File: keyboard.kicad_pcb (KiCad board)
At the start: 2 copper layers, 359.9 x 94.6 mm, 210 parts, among them IC1 ATMEGA32U4, J1 USB C, X1 ASX3F

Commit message: Add an additional led to PCB
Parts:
- added D102: WS2812B, LED_SMD:LED_WS2812B_PLCC4_5.0x5.0mm_P3.2mm, B.Cu at (408.9, 121.2)
- moved D91 18.2 mm to (81.3, 119.4)
- moved D8 11.5 mm to (102.0, 105.2)
- moved D89 10.3 mm to (352.1, 154.2)
- moved D90 9.73 mm to (119.1, 140.5)
- moved D34 6.42 mm to (191.6, 135.6)
- moved D100 5.68 mm to (233.9, 140.5)
- moved D99 4.72 mm to (290.8, 140.3)
- moved D98 3.63 mm to (349.2, 140.3)
- moved C6 1.35 mm to (169.7, 155.3)
- moved D101 0.54 mm to (178.8, 140.5)
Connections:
- D97 pad 2: Net-(D97-Pad2) -> Net-(D102-Pad4)
- D98 pad 4: Net-(D97-Pad2) -> Net-(D102-Pad2)
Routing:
- net VCC: track 568.0 -> 912.6 mm, vias 8 -> 18
- net Net-(D102-Pad2): track 0.00 -> 70.3 mm, vias 0 -> 2
- net Net-(D100-Pad4): track 0.00 -> 57.9 mm, vias 0 -> 2
- net Net-(D98-Pad2): track 0.00 -> 54.8 mm, vias 0 -> 2
- net Net-(D102-Pad4): track 0.00 -> 49.1 mm
- net Net-(D100-Pad2): track 0.00 -> 47.8 mm, vias 0 -> 1
- net /col16: track 348.1 -> 333.7 mm, vias 4 -> 3
- net Net-(D8-Pad2): track 16.2 -> 5.02 mm
- net Net-(D89-Pad2): track 4.11 -> 14.8 mm
- net /col15: track 306.8 -> 297.4 mm, vias 4 -> 3
- net /row4: track 418.3 -> 410.0 mm
- net Net-(D34-Pad2): track 15.8 -> 10.5 mm
- net /col14: track 308.1 -> 303.5 mm
- net /col4: track 100.1 -> 102.4 mm
- net /col2: track 160.3 -> 162.4 mm
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
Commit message: Finish connecting all leds
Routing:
- net Net-(D91-Pad2): track 0.00 -> 65.2 mm, vias 0 -> 2
- net Net-(D90-Pad2): track 0.00 -> 40.4 mm, vias 0 -> 2
- net /leds: track 0.00 -> 36.2 mm, vias 0 -> 2
- net /col16: track 333.7 -> 343.1 mm, vias 3 -> 4
- net /col15: track 297.4 -> 306.0 mm, vias 3 -> 4
- net Net-(D100-Pad2): track 47.8 -> 52.3 mm, vias 1 -> 2
- net /col4: track 102.4 -> 104.8 mm

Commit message: Make first row linear
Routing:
- net /row1: track 459.8 -> 406.4 mm

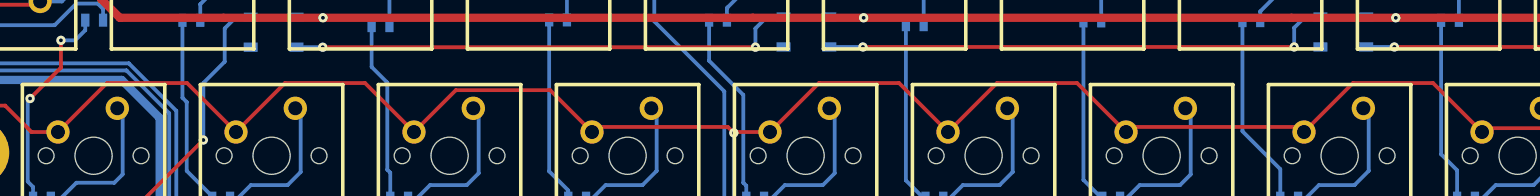
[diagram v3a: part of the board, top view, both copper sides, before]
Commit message: Make second row linear
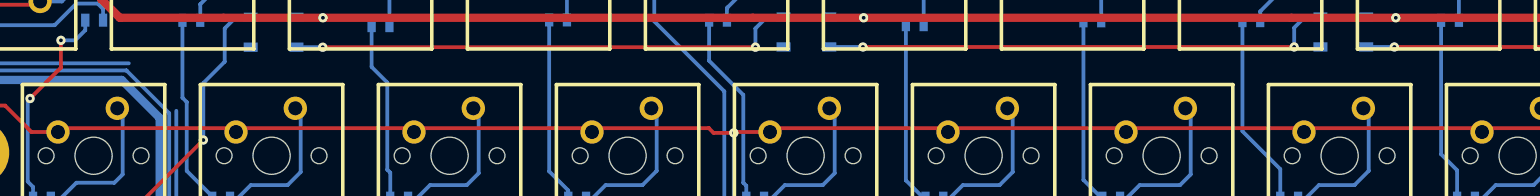
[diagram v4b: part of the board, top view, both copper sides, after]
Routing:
- net /row2: track 409.4 -> 386.6 mm
- net Net-(IC1-Pad4): track 123.8 -> 116.6 mm
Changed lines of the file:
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@@
     (thickness 1.6002)
     (drawings 87)
-    (tracks 1705)
+    (tracks 1713)
     (zones 0)
     (modules 211)
@@
   (segment (start 324.38848 70.866) (end 324.8025 71.28002) (width 0.4064) (layer F.Cu) (net 71))
   (segment (start 296.926 70.866) (end 324.38848 70.866) (width 0.4064) (layer F.Cu) (net 71))
-  (segment (start 96.2025 90.33002) (end 101.44252 85.09) (width 0.4064) (layer F.Cu) (net 72))
-  (segment (start 110.01248 85.09) (end 115.2525 90.33002) (width 0.4064) (layer F.Cu) (net 72))
-  (segment (start 205.26248 85.09) (end 210.5025 90.33002) (width 0.4064) (layer F.Cu) (net 72))
-  (segment (start 120.49252 85.09) (end 129.06248 85.09) (width 0.4064) (layer F.Cu) (net 72))
-  (segment (start 129.06248 85.09) (end 134.3025 90.33002) (width 0.4064) (layer F.Cu) (net 72))
-  (segment (start 138.78052 85.852) (end 148.87448 85.852) (width 0.4064) (layer F.Cu) (net 72))
-  (segment (start 148.87448 85.852) (end 153.3525 90.33002) (width 0.4064) (layer F.Cu) (net 72))
-  (segment (start 191.4525 90.33002) (end 196.69252 85.09) (width 0.4064) (layer F.Cu) (net 72))
-  (segment (start 101.44252 85.09) (end 110.01248 85.09) (width 0.4064) (layer F.Cu) (net 72))
-  (segment (start 134.3025 90.33002) (end 138.78052 85.852) (width 0.4064) (layer F.Cu) (net 72))
-  (segment (start 196.69252 85.09) (end 205.26248 85.09) (width 0.4064) (layer F.Cu) (net 72))
-  (segment (start 172.4025 90.33002) (end 177.64252 85.09) (width 0.4064) (layer F.Cu) (net 72))
-  (segment (start 186.21248 85.09) (end 191.4525 90.33002) (width 0.4064) (layer F.Cu) (net 72))
-  (segment (start 177.64252 85.09) (end 186.21248 85.09) (width 0.4064) (layer F.Cu) (net 72))
-  (segment (start 115.2525 90.33002) (end 120.49252 85.09) (width 0.4064) (layer F.Cu) (net 72))
-  (segment (start 234.79252 85.09) (end 243.36248 85.09) (width 0.4064) (layer F.Cu) (net 72))
-  (segment (start 229.5525 90.33002) (end 234.79252 85.09) (width 0.4064) (layer F.Cu) (net 72))
-  (segment (start 243.36248 85.09) (end 248.6025 90.33002) (width 0.4064) (layer F.Cu) (net 72))
   (segment (start 93.37802 90.33002) (end 96.2025 90.33002) (width 0.4064) (layer F.Cu) (net 72))
   (segment (start 72.39 90.33002) (end 72.93102 89.789) (width 0.4064) (layer F.Cu) (net 72))
@@
   (segment (start 172.4025 90.33002) (end 168.62298 90.33002) (width 0.4064) (layer F.Cu) (net 72))
   (segment (start 168.529 90.424) (end 168.62298 90.33002) (width 0.4064) (layer F.Cu) (net 72))
-  (segment (start 153.89352 89.789) (end 167.894 89.789) (width 0.4064) (layer F.Cu) (net 72))
-  (segment (start 167.894 89.789) (end 168.529 90.424) (width 0.4064) (layer F.Cu) (net 72))
-  (segment (start 153.3525 90.33002) (end 153.89352 89.789) (width 0.4064) (layer F.Cu) (net 72))
-  (segment (start 211.04352 89.789) (end 229.01148 89.789) (width 0.4064) (layer F.Cu) (net 72))
-  (segment (start 229.01148 89.789) (end 229.5525 90.33002) (width 0.4064) (layer F.Cu) (net 72))
   (segment (start 210.5025 90.33002) (end 211.04352 89.789) (width 0.4064) (layer F.Cu) (net 72))
   (segment (start 249.01652 89.916) (end 267.23848 89.916) (width 0.4064) (layer F.Cu) (net 72))
@@
   (segment (start 390.0805 89.9795) (end 390.525 90.424) (width 0.4064) (layer F.Cu) (net 72))
   (segment (start 372.0465 89.9795) (end 390.0805 89.9795) (width 0.4064) (layer F.Cu) (net 72))
+  (segment (start 96.2025 90.33002) (end 96.2025 90.2335) (width 0.4064) (layer F.Cu) (net 72))
+  (segment (start 96.2025 90.2335) (end 96.52 89.916) (width 0.4064) (layer F.Cu) (net 72))
+  (segment (start 114.83848 89.916) (end 115.2525 90.33002) (width 0.4064) (layer F.Cu) (net 72))
+  (segment (start 96.52 89.916) (end 114.83848 89.916) (width 0.4064) (layer F.Cu) (net 72))
+  (segment (start 248.6025 90.33002) (end 248.06402 90.33002) (width 0.4064) (layer F.Cu) (net 72))
+  (segment (start 248.06402 90.33002) (end 247.65 89.916) (width 0.4064) (layer F.Cu) (net 72))
+  (segment (start 247.65 89.916) (end 229.96652 89.916) (width 0.4064) (layer F.Cu) (net 72))
+  (segment (start 229.96652 89.916) (end 229.5525 90.33002) (width 0.4064) (layer F.Cu) (net 72))
+  (segment (start 229.5525 90.33002) (end 229.52202 90.33002) (width 0.4064) (layer F.Cu) (net 72))
+  (segment (start 229.52202 90.33002) (end 229.108 89.916) (width 0.4064) (layer F.Cu) (net 72))
+  (segment (start 210.91652 89.916) (end 210.5025 90.33002) (width 0.4064) (layer F.Cu) (net 72))
+  (segment (start 229.108 89.916) (end 210.91652 89.916) (width 0.4064) (layer F.Cu) (net 72))
+  (segment (start 210.5025 90.33002) (end 209.96402 90.33002) (width 0.4064) (layer F.Cu) (net 72))
+  (segment (start 209.96402 90.33002) (end 209.55 89.916) (width 0.4064) (layer F.Cu) (net 72))
+  (segment (start 191.86652 89.916) (end 191.4525 90.33002) (width 0.4064) (layer F.Cu) (net 72))
+  (segment (start 209.55 89.916) (end 191.86652 89.916) (width 0.4064) (layer F.Cu) (net 72))
+  (segment (start 172.81652 89.916) (end 172.4025 90.33002) (width 0.4064) (layer F.Cu) (net 72))
+  (segment (start 190.754 89.916) (end 172.81652 89.916) (width 0.4064) (layer F.Cu) (net 72))
+  (segment (start 191.16802 90.33002) (end 190.754 89.916) (width 0.4064) (layer F.Cu) (net 72))
+  (segment (start 191.4525 90.33002) (end 191.16802 90.33002) (width 0.4064) (layer F.Cu) (net 72))
+  (segment (start 153.76652 89.916) (end 153.3525 90.33002) (width 0.4064) (layer F.Cu) (net 72))
+  (segment (start 165.862 89.916) (end 153.76652 89.916) (width 0.4064) (layer F.Cu) (net 72))
+  (segment (start 166.37 90.424) (end 165.862 89.916) (width 0.4064) (layer F.Cu) (net 72))
+  (segment (start 168.529 90.424) (end 166.37 90.424) (width 0.4064) (layer F.Cu) (net 72))
+  (segment (start 134.71652 89.916) (end 134.3025 90.33002) (width 0.4064) (layer F.Cu) (net 72))
+  (segment (start 152.908 89.916) (end 134.71652 89.916) (width 0.4064) (layer F.Cu) (net 72))
+  (segment (start 153.32202 90.33002) (end 152.908 89.916) (width 0.4064) (layer F.Cu) (net 72))
+  (segment (start 153.3525 90.33002) (end 153.32202 90.33002) (width 0.4064) (layer F.Cu) (net 72))
+  (segment (start 134.3025 90.33002) (end 134.01802 90.33002) (width 0.4064) (layer F.Cu) (net 72))
+  (segment (start 134.01802 90.33002) (end 133.604 89.916) (width 0.4064) (layer F.Cu) (net 72))
+  (segment (start 115.66652 89.916) (end 115.2525 90.33002) (width 0.4064) (layer F.Cu) (net 72))
+  (segment (start 133.604 89.916) (end 115.66652 89.916) (width 0.4064) (layer F.Cu) (net 72))
   (segment (start 100.69068 108.95584) (end 100.965 109.38002) (width 0.4064) (layer F.Cu) (net 73))
   (segment (start 106.20502 104.14) (end 114.77498 104.14) (width 0.4064) (layer F.Cu) (net 73))
@@
   (segment (start 159.68472 139.99972) (end 157.90926 138.22426) (width 0.4064) (layer B.Cu) (net 76))
   (segment (start 159.68472 139.99972) (end 159.68472 143.19504) (width 0.4064) (layer B.Cu) (net 76))
-  (segment (start 108.86694 88.05926) (end 103.78694 82.97926) (width 0.4064) (layer B.Cu) (net 76))
   (segment (start 114.45494 106.09326) (end 114.45494 116.76126) (width 0.4064) (layer B.Cu) (net 76))
   (segment (start 114.45494 116.76126) (end 124.10694 126.41326) (width 0.4064) (layer B.Cu) (net 76))

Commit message: Make third row linear
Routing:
- net /row3: track 438.0 -> 415.5 mm
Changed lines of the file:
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@@
   (layers
     (0 F.Cu signal)
-    (31 B.Cu signal)
+    (31 B.Cu signal hide)
     (32 B.Adhes user hide)
     (33 F.Adhes user hide)
@@
   (segment (start 133.604 89.916) (end 115.66652 89.916) (width 0.4064) (layer F.Cu) (net 72))
   (segment (start 100.69068 108.95584) (end 100.965 109.38002) (width 0.4064) (layer F.Cu) (net 73))
-  (segment (start 106.20502 104.14) (end 114.77498 104.14) (width 0.4064) (layer F.Cu) (net 73))
-  (segment (start 100.965 109.38002) (end 106.20502 104.14) (width 0.4064) (layer F.Cu) (net 73))
-  (segment (start 133.82498 104.14) (end 139.065 109.38002) (width 0.4064) (layer F.Cu) (net 73))
-  (segment (start 286.22498 104.14) (end 291.465 109.38002) (width 0.4064) (layer F.Cu) (net 73))
-  (segment (start 258.60502 104.14) (end 267.17498 104.14) (width 0.4064) (layer F.Cu) (net 73))
-  (segment (start 277.65502 104.14) (end 286.22498 104.14) (width 0.4064) (layer F.Cu) (net 73))
-  (segment (start 253.365 109.38002) (end 258.60502 104.14) (width 0.4064) (layer F.Cu) (net 73))
   (segment (start 101.522711 109.601) (end 100.965 109.38002) (width 0.4064) (layer F.Cu) (net 73))
   (segment (start 100.965 109.38002) (end 100.69068 108.93552) (width 0.4064) (layer F.Cu) (net 73))
-  (segment (start 125.25502 104.14) (end 133.82498 104.14) (width 0.4064) (layer F.Cu) (net 73))
-  (segment (start 114.77498 104.14) (end 120.015 109.38002) (width 0.4064) (layer F.Cu) (net 73))
-  (segment (start 267.17498 104.14) (end 272.415 109.38002) (width 0.4064) (layer F.Cu) (net 73))
-  (segment (start 120.015 109.38002) (end 125.25502 104.14) (width 0.4064) (layer F.Cu) (net 73))
-  (segment (start 272.415 109.38002) (end 277.65502 104.14) (width 0.4064) (layer F.Cu) (net 73))
   (segment (start 74.77252 109.38002) (end 74.77252 108.42752) (width 0.4064) (layer F.Cu) (net 73) (status 30))
   (segment (start 322.42125 109.37875) (end 322.707 109.6645) (width 0.4064) (layer F.Cu) (net 73))
-  (segment (start 171.56176 116.06276) (end 171.577 116.04752) (width 0.4064) (layer B.Cu) (net 73))
   (segment (start 167.05326 120.57126) (end 171.56176 116.06276) (width 0.4064) (layer B.Cu) (net 73))
   (segment (start 171.577 108.966) (end 176.75098 108.966) (width 0.4064) (layer F.Cu) (net 73))
   (segment (start 176.75098 108.966) (end 177.165 109.38002) (width 0.4064) (layer F.Cu) (net 73))
-  (segment (start 158.52902 108.966) (end 171.577 108.966) (width 0.4064) (layer F.Cu) (net 73))
+  (segment (start 158.52902 108.966) (end 171.45 108.966) (width 0.4064) (layer F.Cu) (net 73))
   (segment (start 158.115 109.38002) (end 158.52902 108.966) (width 0.4064) (layer F.Cu) (net 73))
-  (segment (start 171.56176 108.56976) (end 171.45 108.458) (width 0.4064) (layer B.Cu) (net 73))
-  (via (at 171.45 108.458) (size 1) (layers F.Cu B.Cu) (net 73))
-  (segment (start 171.45 108.458) (end 171.577 108.585) (width 0.4064) (layer F.Cu) (net 73))
-  (segment (start 171.577 108.585) (end 171.577 108.966) (width 0.4064) (layer F.Cu) (net 73))
-  (segment (start 171.56176 116.06276) (end 171.56176 108.56976) (width 0.4064) (layer B.Cu) (net 73))
   (segment (start 234.72902 108.966) (end 252.95098 108.966) (width 0.4064) (layer F.Cu) (net 73))
   (segment (start 252.95098 108.966) (end 253.365 109.38002) (width 0.4064) (layer F.Cu) (net 73))
@@
   (segment (start 157.70098 108.966) (end 158.115 109.38002) (width 0.4064) (layer F.Cu) (net 73))
   (segment (start 139.065 109.38002) (end 139.47902 108.966) (width 0.4064) (layer F.Cu) (net 73))
-  (segment (start 74.77252 109.38002) (end 76.2 107.95254) (width 0.4064) (layer F.Cu) (net 73))
-  (segment (start 76.2 107.95254) (end 78.73746 107.95254) (width 0.4064) (layer F.Cu) (net 73))
-  (segment (start 80.38592 109.601) (end 81.661 109.601) (width 0.4064) (layer F.Cu) (net 73))
-  (segment (start 78.73746 107.95254) (end 80.38592 109.601) (width 0.4064) (layer F.Cu) (net 73))
-  (segment (start 81.661 109.601) (end 101.522711 109.601) (width 0.4064) (layer F.Cu) (net 73))
-  (segment (start 321.6275 108.585) (end 322.42125 109.37875) (width 0.4064) (layer F.Cu) (net 73))
-  (segment (start 312.42 108.585) (end 321.6275 108.585) (width 0.4064) (layer F.Cu) (net 73))
-  (segment (start 307.975 104.14) (end 312.42 108.585) (width 0.4064) (layer F.Cu) (net 73))
-  (segment (start 296.70502 104.14) (end 307.975 104.14) (width 0.4064) (layer F.Cu) (net 73))
-  (segment (start 291.465 109.38002) (end 296.70502 104.14) (width 0.4064) (layer F.Cu) (net 73))
   (segment (start 164.48532 123.1392) (end 165.27526 122.34926) (width 0.4064) (layer B.Cu) (net 73))
   (segment (start 165.27526 122.34926) (end 164.719 122.90552) (width 0.4064) (layer B.Cu) (net 73))
@@
   (segment (start 410.1084 71.882) (end 409.448 71.2216) (width 0.4064) (layer F.Cu) (net 73))
   (segment (start 410.1084 75.6412) (end 410.1084 71.882) (width 0.4064) (layer F.Cu) (net 73))
+  (segment (start 171.45 108.966) (end 171.577 108.966) (width 0.4064) (layer F.Cu) (net 73))
+  (via (at 171.45 108.966) (size 1) (drill 0.4) (layers F.Cu B.Cu) (net 73))
+  (segment (start 171.56176 109.07776) (end 171.45 108.966) (width 0.4064) (layer B.Cu) (net 73))
+  (segment (start 171.56176 116.06276) (end 171.56176 109.07776) (width 0.4064) (layer B.Cu) (net 73))
+  (segment (start 74.77252 109.38002) (end 74.77252 109.37748) (width 0.4064) (layer F.Cu) (net 73))
+  (segment (start 74.77252 109.37748) (end 75.184 108.966) (width 0.4064) (layer F.Cu) (net 73))
+  (segment (start 100.55098 108.966) (end 100.965 109.38002) (width 0.4064) (layer F.Cu) (net 73))
+  (segment (start 75.184 108.966) (end 100.55098 108.966) (width 0.4064) (layer F.Cu) (net 73))
+  (segment (start 100.965 109.38002) (end 100.965 109.347) (width 0.4064) (layer F.Cu) (net 73))
+  (segment (start 100.965 109.347) (end 101.346 108.966) (width 0.4064) (layer F.Cu) (net 73))
+  (segment (start 119.60098 108.966) (end 120.015 109.38002) (width 0.4064) (layer F.Cu) (net 73))
+  (segment (start 101.346 108.966) (end 119.60098 108.966) (width 0.4064) (layer F.Cu) (net 73))
+  (segment (start 120.015 109.38002) (end 120.48998 109.38002) (width 0.4064) (layer F.Cu) (net 73))
+  (segment (start 120.48998 109.38002) (end 120.904 108.966) (width 0.4064) (layer F.Cu) (net 73))
+  (segment (start 138.65098 108.966) (end 139.065 109.38002) (width 0.4064) (layer F.Cu) (net 73))
+  (segment (start 120.904 108.966) (end 138.65098 108.966) (width 0.4064) (layer F.Cu) (net 73))
+  (segment (start 253.365 109.38002) (end 253.58598 109.38002) (width 0.4064) (layer F.Cu) (net 73))
+  (segment (start 253.58598 109.38002) (end 254 108.966) (width 0.4064) (layer F.Cu) (net 73))
+  (segment (start 272.00098 108.966) (end 272.415 109.38002) (width 0.4064) (layer F.Cu) (net 73))
+  (segment (start 254 108.966) (end 272.00098 108.966) (width 0.4064) (layer F.Cu) (net 73))
+  (segment (start 272.415 109.38002) (end 273.14398 109.38002) (width 0.4064) (layer F.Cu) (net 73))
+  (segment (start 273.14398 109.38002) (end 273.558 108.966) (width 0.4064) (layer F.Cu) (net 73))
+  (segment (start 291.05098 108.966) (end 291.465 109.38002) (width 0.4064) (layer F.Cu) (net 73))
+  (segment (start 273.558 108.966) (end 291.05098 108.966) (width 0.4064) (layer F.Cu) (net 73))
+  (segment (start 291.465 109.38002) (end 291.465 109.347) (width 0.4064) (layer F.Cu) (net 73))
+  (segment (start 291.465 109.347) (end 291.846 108.966) (width 0.4064) (layer F.Cu) (net 73))
+  (segment (start 322.0085 108.966) (end 322.42125 109.37875) (width 0.4064) (layer F.Cu) (net 73))
+  (segment (start 291.846 108.966) (end 322.0085 108.966) (width 0.4064) (layer F.Cu) (net 73))
   (segment (start 191.93002 123.19) (end 186.69 128.43002) (width 0.4064) (layer F.Cu) (net 74))
   (segment (start 200.49998 123.19) (end 191.93002 123.19) (width 0.4064) (layer F.Cu) (net 74))
